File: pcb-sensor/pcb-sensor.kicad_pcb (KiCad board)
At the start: 2 copper layers, 86 x 86 mm, 28 parts, among them J1 Conn_02x06_Counter_Clockwise, J2 Conn_01x03, J3 Conn_01x01, J4 Conn_01x05, J5 Conn_01x02, J6 Conn_01x03, J7 Conn_01x01, J8 Conn_01x01, U1 LM340MP, U2 SFH617A-2X009T, U4 SFH617A-2X009T

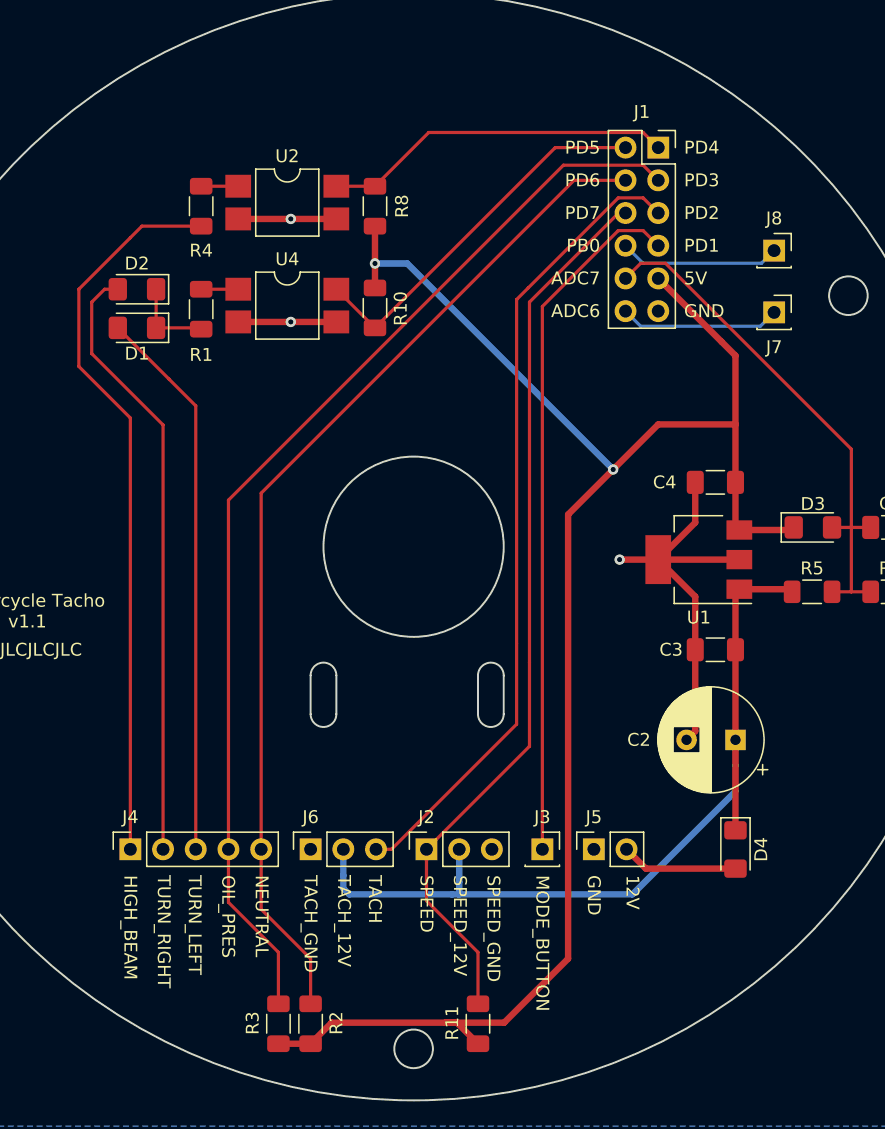
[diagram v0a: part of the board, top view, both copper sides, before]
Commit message: resolves #26: protection diodes
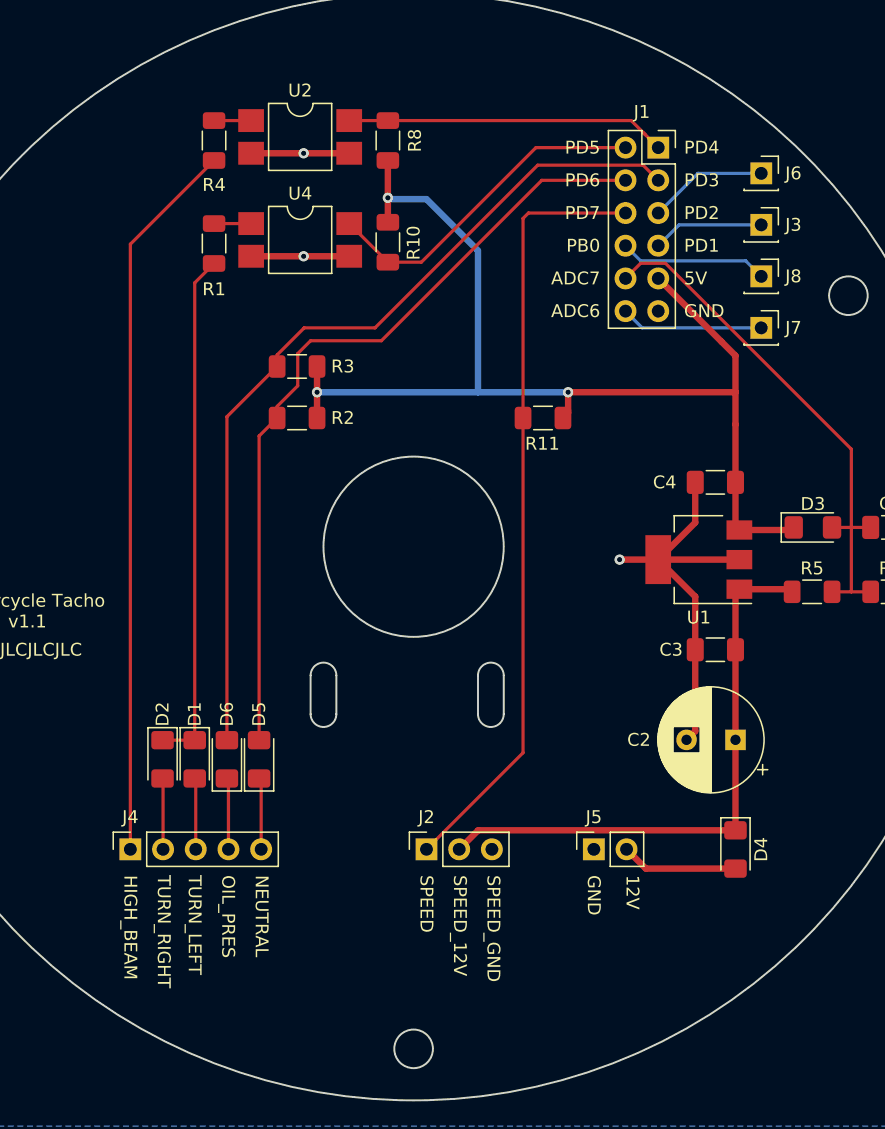
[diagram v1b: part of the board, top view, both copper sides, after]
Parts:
- added D5: D, Diode_SMD:D_1206_3216Metric_Pad1.42x1.75mm_HandSolder, F.Cu at (138.0, 116.5)
- added D6: D, Diode_SMD:D_1206_3216Metric_Pad1.42x1.75mm_HandSolder, F.Cu at (135.5, 116.5)
- J6: value Conn_01x03 -> Conn_01x01; footprint Connector_PinSocket_2.54mm:PinSocket_1x03_P2.54mm_Vertical -> Connector_PinSocket_2.54mm:PinSocket_1x01_P2.54mm_Vertical
- R11: value 10k -> 1k
- moved J6 63.1 mm to (177.0, 71.0), turned to 0 degrees
- moved J3 51.4 mm to (177.0, 75.0)
- moved R3 51.1 mm to (140.9, 86.0), turned to 180 degrees
- moved R11 47.3 mm to (160.1, 90.0), turned to 180 degrees
- moved R2 47.1 mm to (140.9, 90.0), turned to 180 degrees
- moved D2 36.6 mm to (130.5, 116.5), turned to -90 degrees
- moved D1 33.8 mm to (133.0, 116.5), turned to -90 degrees
- moved R10 5.20 mm to (148.0, 76.3)
- moved R1 5.20 mm to (134.5, 76.5)
- moved R4 5.20 mm to (134.5, 68.5)
- moved R8 5.20 mm to (148.0, 68.5)
- moved U2 5.20 mm to (141.2, 68.2)
- moved U4 5.20 mm to (141.2, 76.2)
- moved J8 2.24 mm to (177.0, 79.0)
- moved J7 1.56 mm to (177.0, 83.0)
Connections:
- net /MODE_BUTTON renamed /PD1
- J1 pad 3: /OIL_PRESSURE -> /PD3
- J1 pad 4: /NEUTRAL -> /PD6
- J6 pad 1: GND -> /PD2
- R2 pad 2: /NEUTRAL -> /PD6
- R3 pad 2: /OIL_PRESSURE -> /PD3
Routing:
- net /OIL_PRESSURE: track 85.4 -> 5.55 mm
- net /NEUTRAL: track 79.6 -> 5.57 mm
- net /PD3: track 0.00 -> 67.7 mm
- net /PD6: track 0.00 -> 62.3 mm
- net /PD2: track 62.7 -> 9.28 mm
- net +5V: track 135.2 -> 89.6 mm, vias 2 -> 3
- net /PD1: track 54.1 -> 8.67 mm
- net /TURN_SIGNAL_RIGHT: track 47.2 -> 5.52 mm
- net /TURN_SIGNAL_LEFT: track 43.0 -> 5.53 mm
- net Net-(D1-Pad1): track 6.54 -> 40.1 mm
- net +12V: track 67.6 -> 45.1 mm
- net /PD7: track 69.8 -> 60.2 mm
- net /PD5: track 29.5 -> 26.4 mm
- net /PD4: track 27.2 -> 25.1 mm
- net /ADC6: track 12.5 -> 11.1 mm
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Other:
- board text removed: "MODE_BUTTON"
- board text removed: "TACH"
- board text removed: "TACH_12V"
- board text removed: "TACH_GND"

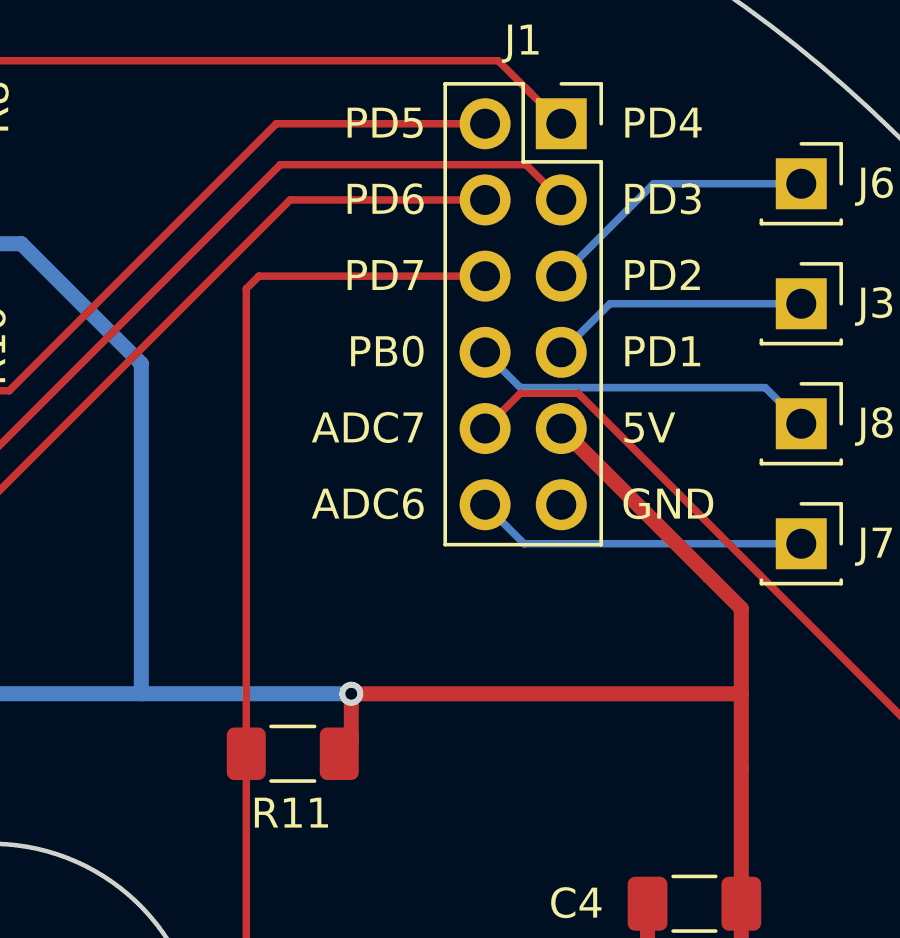
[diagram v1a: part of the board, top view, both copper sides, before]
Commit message: resolves #17: interrupt pin
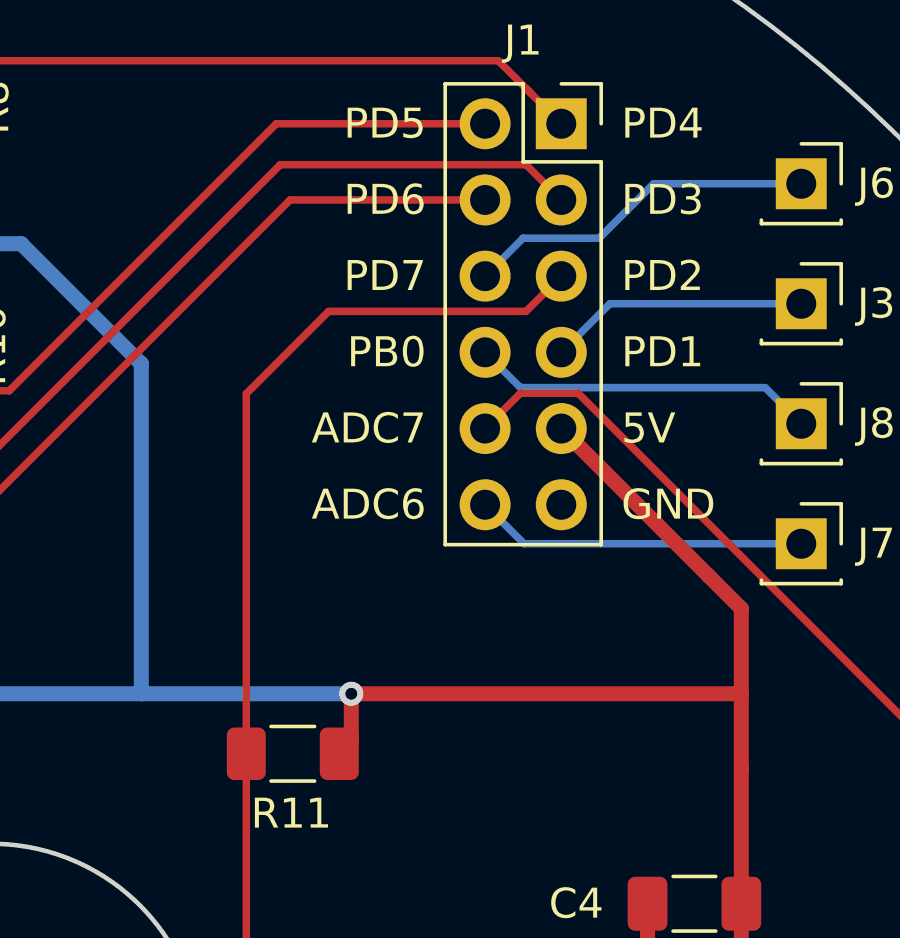
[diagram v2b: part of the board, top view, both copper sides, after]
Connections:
- J2 pad 1: /PD7 -> /PD2
- J6 pad 1: /PD2 -> /PD7
- R11 pad 2: /PD7 -> /PD2
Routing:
- net /PD2: track 9.28 -> 60.7 mm
- net /PD7: track 60.2 -> 11.8 mm
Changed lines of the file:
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@@
       (net 4 "+5V") (pintype "passive"))
     (pad "2" smd roundrect locked (at 1.55 0 180) (size 1.3 1.75) (layers "F.Cu" "F.Paste" "F.Mask") (roundrect_rratio 0.1923076923)
-      (net 19 "/PD7") (pintype "passive"))
+      (net 17 "/PD2") (pintype "passive"))
     (model "${KICAD6_3DMODEL_DIR}/Resistor_SMD.3dshapes/R_1206_3216Metric.wrl"
       (offset (xyz 0 0 0))
@@
     (fp_line (start 0.635 -1.27) (end 1.27 -0.635) (layer "F.Fab") (width 0.1))
     (pad "1" thru_hole rect locked (at 0 0 90) (size 1.7 1.7) (drill 1) (layers *.Cu *.Mask)
-      (net 19 "/PD7") (pinfunction "Pin_1") (pintype "passive"))
+      (net 17 "/PD2") (pinfunction "Pin_1") (pintype "passive"))
     (pad "2" thru_hole oval locked (at 0 2.54 90) (size 1.7 1.7) (drill 1) (layers *.Cu *.Mask)
       (net 16 "+12V") (pinfunction "Pin_2") (pintype "passive"))
@@
     (fp_line (start 1.27 -0.635) (end 1.27 1.27) (layer "F.Fab") (width 0.1))
     (pad "1" thru_hole rect (at 0 0) (size 1.7 1.7) (drill 1) (layers *.Cu *.Mask)
-      (net 17 "/PD2") (pinfunction "Pin_1") (pintype "passive"))
+      (net 19 "/PD7") (pinfunction "Pin_1") (pintype "passive"))
   )
   (footprint "Diode_SMD:D_1206_3216Metric_Pad1.42x1.75mm_HandSolder" (layer "F.Cu")
@@
   (segment (start 175.3 103.3) (end 179.2 103.3) (width 0.5) (layer "F.Cu") (net 16))
   (segment (start 179.2 103.3) (end 179.4 103.5) (width 0.5) (layer "F.Cu") (net 16))
-  (segment (start 172.08 71) (end 169 74.08) (width 0.25) (layer "B.Cu") (net 17))
-  (segment (start 177 71) (end 172.08 71) (width 0.25) (layer "B.Cu") (net 17))
+  (segment (start 158.5 78) (end 158.5 90) (width 0.25) (layer "F.Cu") (net 17))
+  (segment (start 167.825 75.255) (end 161.245 75.255) (width 0.25) (layer "F.Cu") (net 17))
+  (segment (start 161.245 75.255) (end 158.5 78) (width 0.25) (layer "F.Cu") (net 17))
+  (segment (start 169 74.08) (end 167.825 75.255) (width 0.25) (layer "F.Cu") (net 17))
+  (segment (start 158.5 116) (end 158.5 90) (width 0.25) (layer "F.Cu") (net 17))
+  (segment (start 151 123.5) (end 158.5 116) (width 0.25) (layer "F.Cu") (net 17))
   (segment (start 175 125) (end 168.04 125) (width 0.5) (layer "F.Cu") (net 18))
   (segment (start 168.04 125) (end 166.54 123.5) (width 0.5) (layer "F.Cu") (net 18))
-  (segment (start 158.5 90) (end 158.5 74.5) (width 0.25) (layer "F.Cu") (net 19))
-  (segment (start 158.92 74.08) (end 166.46 74.08) (width 0.25) (layer "F.Cu") (net 19))
-  (segment (start 158.5 116) (end 158.5 90) (width 0.25) (layer "F.Cu") (net 19))
-  (segment (start 158.5 74.5) (end 158.92 74.08) (width 0.25) (layer "F.Cu") (net 19))
-  (segment (start 151 123.5) (end 158.5 116) (width 0.25) (layer "F.Cu") (net 19))
+  (segment (start 170.265722 72.814278) (end 167.725722 72.814278) (width 0.25) (layer "B.Cu") (net 19))
+  (segment (start 167.725722 72.814278) (end 166.46 74.08) (width 0.25) (layer "B.Cu") (net 19))
+  (segment (start 177 71) (end 172.08 71) (width 0.25) (layer "B.Cu") (net 19))
+  (segment (start 172.08 71) (end 170.265722 72.814278) (width 0.25) (layer "B.Cu") (net 19))
   (segment (start 141 87.5) (end 141 85) (width 0.25) (layer "F.Cu") (net 20))
   (segment (start 138 115.025) (end 138 91.4) (width 0.25) (layer "F.Cu") (net 20))

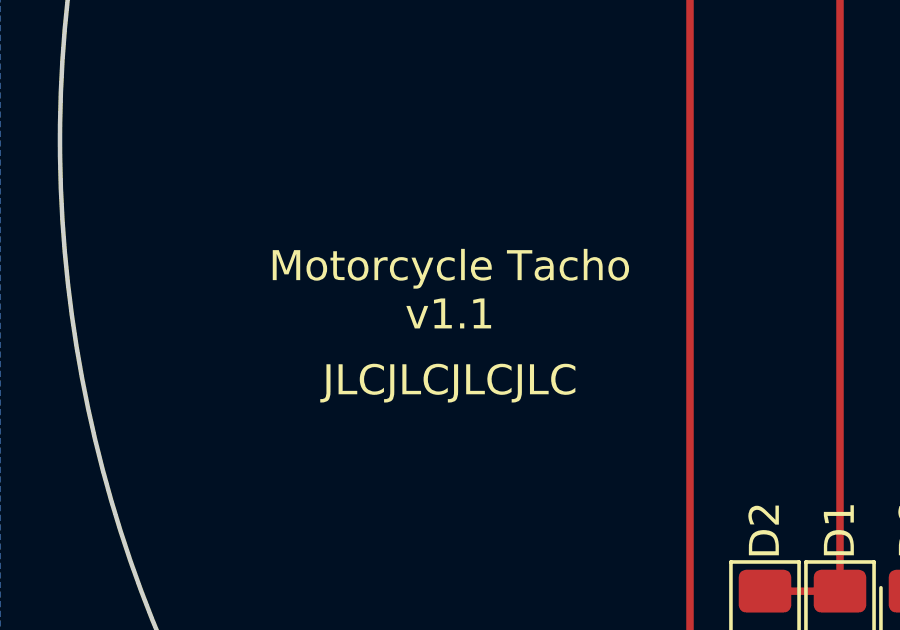
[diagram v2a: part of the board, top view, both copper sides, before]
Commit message: resolves #47: update silkscreen labels
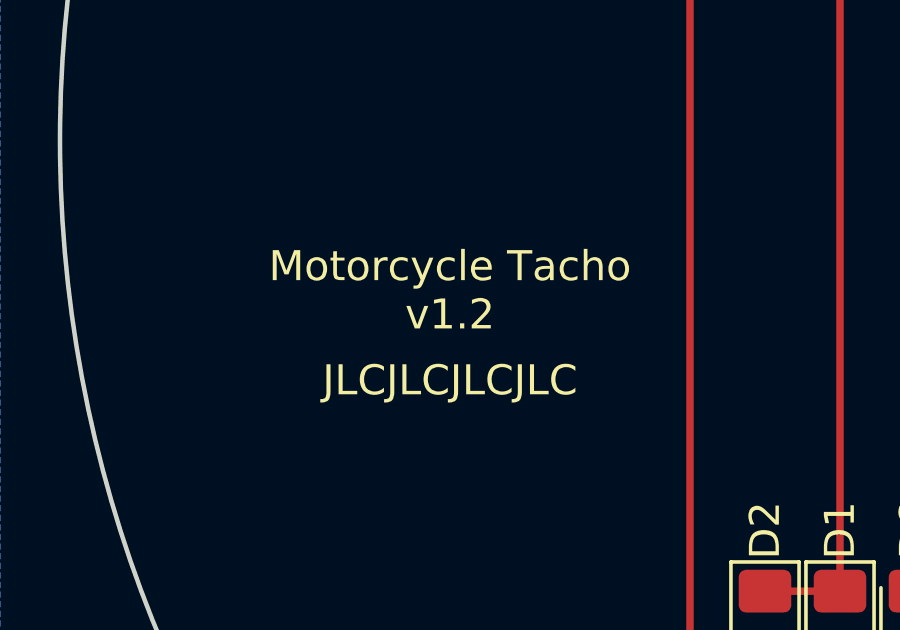
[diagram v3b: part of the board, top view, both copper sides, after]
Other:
- board text added: "Motorcycle Tacho v1.2"
- board text removed: "Motorcycle Tacho v1.1"
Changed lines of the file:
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@@
     (effects (font (size 1 1) (thickness 0.15)) (justify left))
   )
-  (gr_text "Motorcycle Tacho\nv1.1" (at 120 105) (layer "F.SilkS")
+  (gr_text "Motorcycle Tacho\nv1.2" (at 120 105) (layer "F.SilkS")
     (effects (font (size 1 1) (thickness 0.15)))
   )

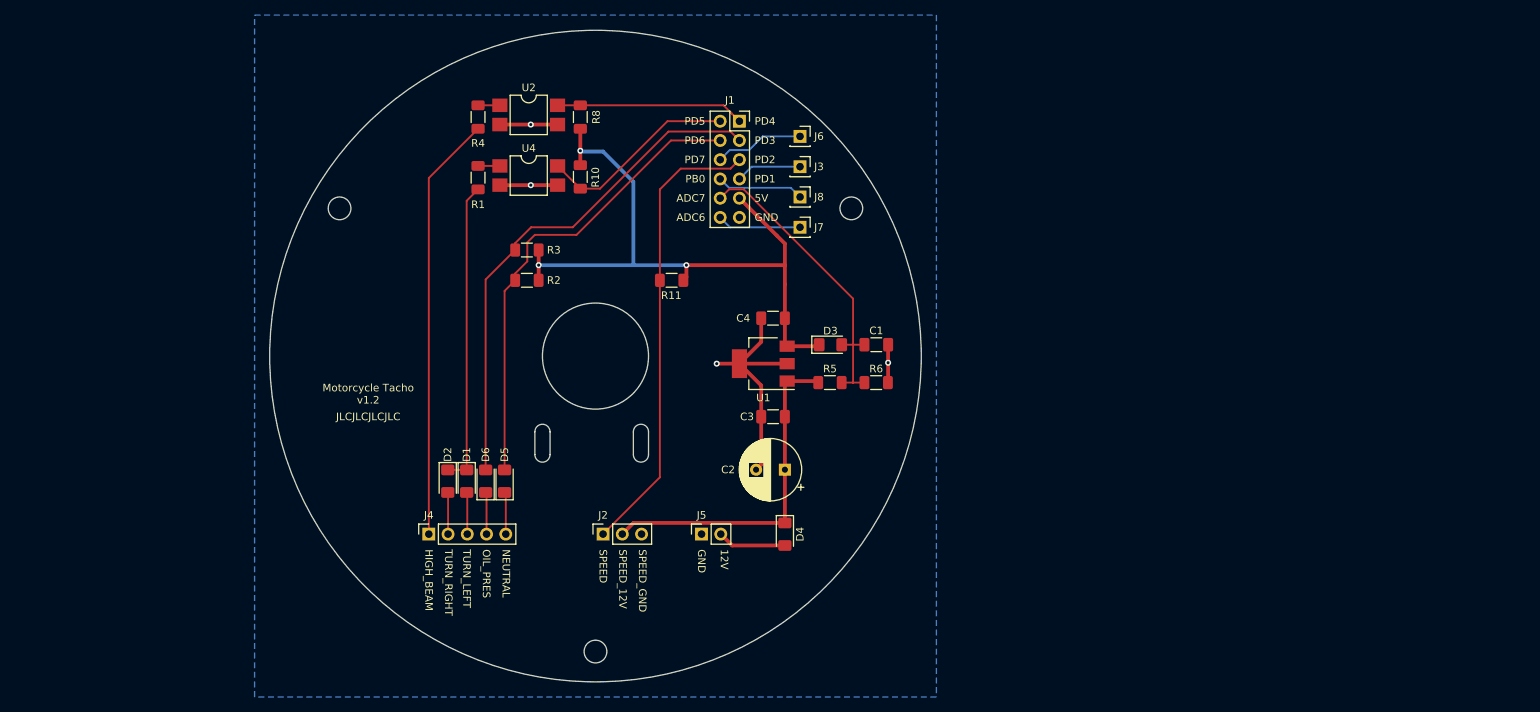
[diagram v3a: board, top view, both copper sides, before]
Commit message: resolves #46: mode button connector
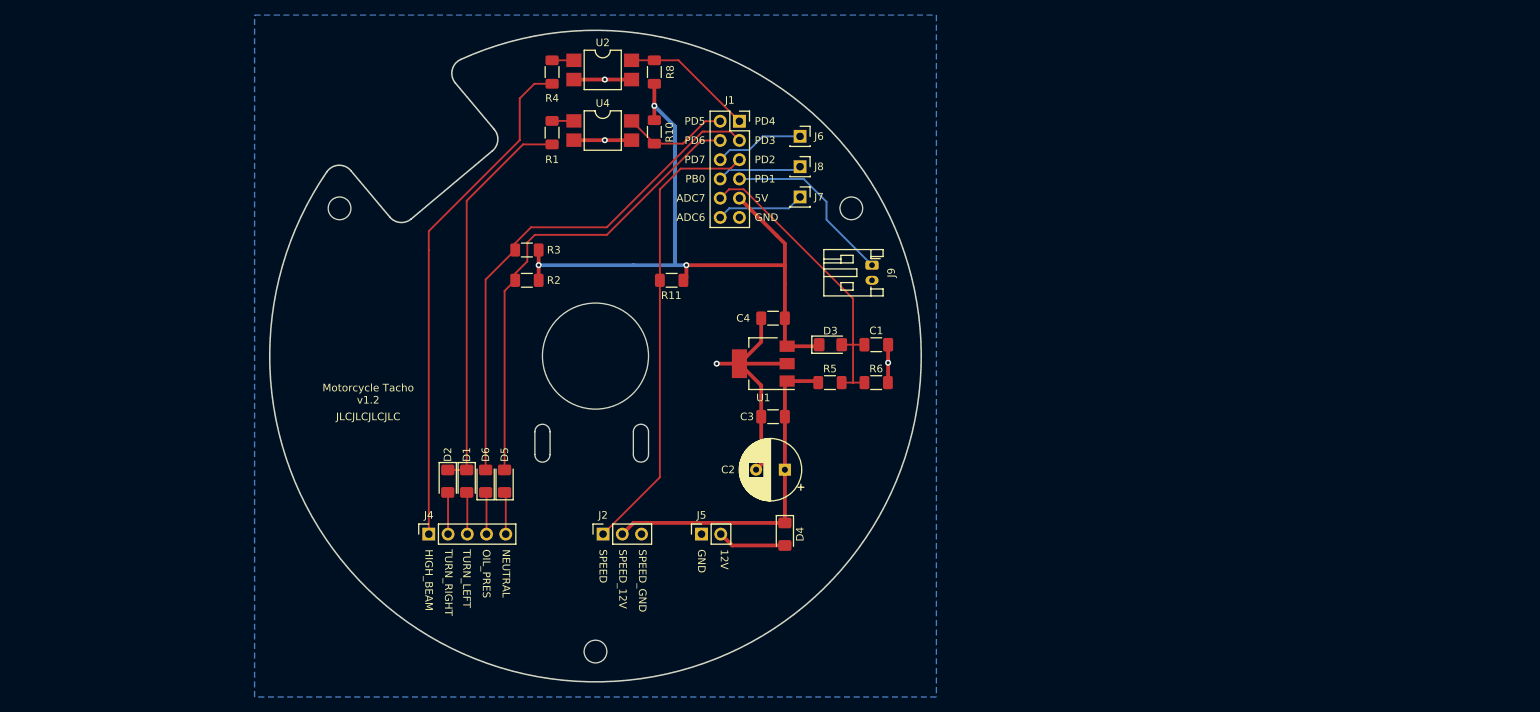
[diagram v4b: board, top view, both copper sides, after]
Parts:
- removed J3: Conn_01x01, Connector_PinSocket_2.54mm:PinSocket_1x01_P2.54mm_Vertical
- added J9: Conn_01x02_Male, Connector_JST:JST_PH_S2B-PH-K_1x02_P2.00mm_Horizontal, F.Cu at (186.5, 88.0)
- moved R4 11.4 mm to (144.3, 62.5)
- moved R8 11.4 mm to (157.8, 62.5)
- moved U2 11.4 mm to (151.0, 62.2)
- moved R1 11.4 mm to (144.3, 70.5)
- moved R10 11.4 mm to (157.8, 70.4)
- moved U4 11.4 mm to (151.0, 70.2)
- moved J7 4.00 mm to (177.0, 79.0)
- moved J8 4.00 mm to (177.0, 75.0)
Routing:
- net /PD1: track 8.67 -> 23.6 mm
- net /PD5: track 26.4 -> 14.2 mm
- net Net-(D1-Pad1): track 40.1 -> 52.4 mm
- net /HIGH_BEAM: track 56.2 -> 67.5 mm
- net /PD4: track 25.1 -> 17.6 mm
- net +5V: track 89.6 -> 92.1 mm
- net /ADC6: track 11.1 -> 11.7 mm
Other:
- outline, holes or cut-outs redrawn
